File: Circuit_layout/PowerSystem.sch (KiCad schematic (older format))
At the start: 6 parts, among them U13 PDQ10-D

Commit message: Backup before pcb relayout
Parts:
- +5DC/DC1: footprint Measurement_Points:Measurement_Point_Round-SMD-Pad_Big -> custom_footprints:trim_pot
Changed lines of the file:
@@
 F 0 "+5DC/DC1" H 5050 1170 50  0000 C CNN
 F 1 "+5DC/DC" H 5050 1100 50  0000 C CNN
-F 2 "Measurement_Points:Measurement_Point_Round-SMD-Pad_Big" H 5250 900 50  0001 C CNN
+F 2 "custom_footprints:trim_pot" H 5250 900 50  0001 C CNN
 F 3 "" H 5250 900 50  0000 C CNN
 	1    5050 900

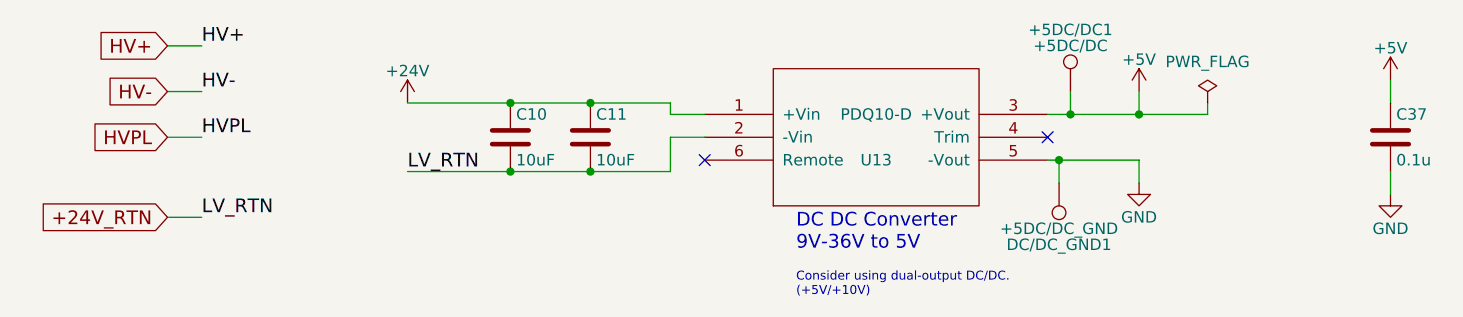
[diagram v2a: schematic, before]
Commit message: Wider traces for DC/DC converter
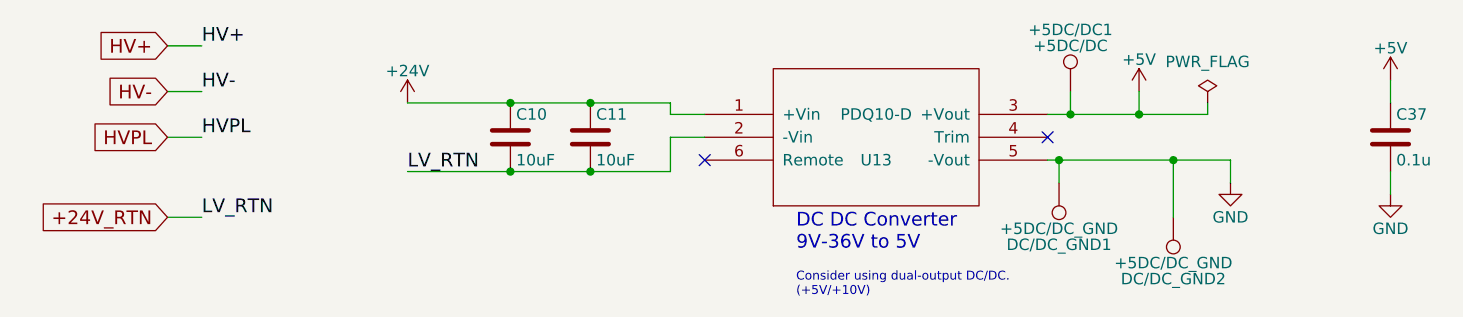
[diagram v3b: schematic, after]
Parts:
- added DC/DC_GND2: +5DC/DC_GND, Measurement_Points:Measurement_Point_Square-SMD-Pad_Big, symbol TEST_1P
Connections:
- net GND: now also DC/DC_GND2.1
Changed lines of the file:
@@
 	5350 1000 5350 900
 Wire Wire Line
-	4950 1200 5350 1200
-Wire Wire Line
-	5350 1200 5350 1300
+	4950 1200 5750 1200
 Wire Wire Line
 	1100 700  1250 700
@@
 L GND #PWR056
 U 1 1 58D1E1EA
-P 5350 1300
-F 0 "#PWR056" H 5350 1050 50  0001 C CNN
-F 1 "GND" H 5350 1150 50  0000 C CNN
-F 2 "" H 5350 1300 50  0000 C CNN
-F 3 "" H 5350 1300 50  0000 C CNN
-	1    5350 1300
+P 5750 1300
+F 0 "#PWR056" H 5750 1050 50  0001 C CNN
+F 1 "GND" H 5750 1150 50  0000 C CNN
+F 2 "" H 5750 1300 50  0000 C CNN
+F 3 "" H 5750 1300 50  0000 C CNN
+	1    5750 1300
 	1    0    0    -1
 $EndComp
@@
 Text Notes 3850 1800 0    39   ~ 0
 Consider using dual-output DC/DC.\n(+5V/+10V)
+Wire Wire Line
+	5750 1200 5750 1300
+$Comp
+L TEST_1P DC/DC_GND2
+U 1 1 5A867BAF
+P 5500 1450
+F 0 "DC/DC_GND2" H 5500 1720 50  0000 C CNN
+F 1 "+5DC/DC_GND" H 5500 1650 50  0000 C CNN
+F 2 "Measurement_Points:Measurement_Point_Square-SMD-Pad_Big" H 5700 1450 50  0001 C CNN
+F 3 "" H 5700 1450 50  0000 C CNN
+	1    5500 1450
+	-1   0    0    1
+$EndComp
+Wire Wire Line
+	5500 1450 5500 1200
+Connection ~ 5500 1200
 $EndSCHEMATC

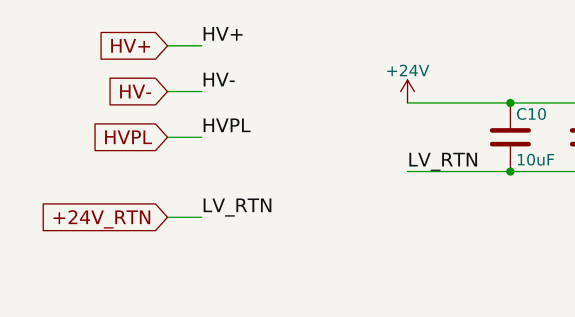
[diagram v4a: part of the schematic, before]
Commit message: Schematic update
Changed schematic to reflect board as assembeled
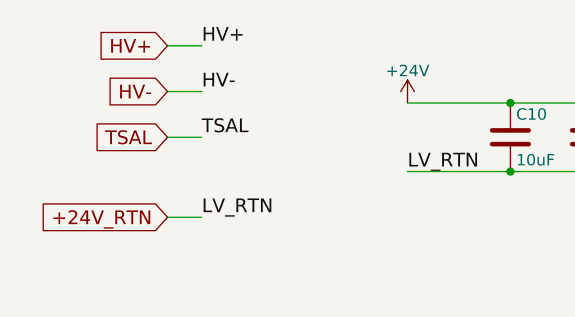
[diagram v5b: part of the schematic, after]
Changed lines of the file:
@@
 LIBS:ftdi
 LIBS:gennum
-LIBS:graphic
 LIBS:hc11
 LIBS:intel
@@
 LIBS:Lattice
 LIBS:linear
-LIBS:logo
 LIBS:maxim
 LIBS:memory
@@
 HV-
 Text Label 1250 1100 0    60   ~ 0
-HVPL
+TSAL
 Text Label 1250 1450 0    60   ~ 0
 LV_RTN
@@
 HV-
 Text GLabel 1100 1100 0    60   Input ~ 0
-HVPL
+TSAL
 Text GLabel 1100 1450 0    60   Input ~ 0
 +24V_RTN
